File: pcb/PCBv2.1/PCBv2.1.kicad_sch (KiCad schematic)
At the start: 50 parts, among them J1 USB4105-GF-A, J2 Conn_01x04, J3 Conn_01x04, J4 Conn_01x08, J5 Conn_01x08, SW1 SW_Push, SW2 SW_Push, U1 STM32F411CEUx, U2 BNO055, U3 AP2112K-3.3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

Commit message: Add button part numbers for pcb
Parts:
- SW1, SW2: footprint (none) -> Button_Switch_SMD:SW_SPST_PTS810; Part Number (none) -> PTS810SJM250SMTRLFS
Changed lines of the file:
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@@
       (effects (font (size 1.27 1.27)) hide)
     )
-    (property "Footprint" "" (id 2) (at 92.71 34.29 0)
-      (effects (font (size 1.27 1.27)) hide)
-    )
-    (property "Datasheet" "~" (id 3) (at 92.71 34.29 0)
-      (effects (font (size 1.27 1.27)) hide)
-    )
-    (property "Part Number" "~" (id 4) (at 92.71 39.37 0)
+    (property "Footprint" "Button_Switch_SMD:SW_SPST_PTS810" (id 2) (at 92.71 34.29 0)
+      (effects (font (size 1.27 1.27)) hide)
+    )
+    (property "Datasheet" "https://www.mouser.com/datasheet/2/240/pts810-3050339.pdf" (id 3) (at 92.71 34.29 0)
+      (effects (font (size 1.27 1.27)) hide)
+    )
+    (property "Part Number" "PTS810SJM250SMTRLFS" (id 4) (at 92.71 39.37 0)
       (effects (font (size 1.27 1.27)) hide)
     )
@@
       (effects (font (size 1.27 1.27)) hide)
     )
-    (property "Footprint" "" (id 2) (at 107.95 16.51 0)
-      (effects (font (size 1.27 1.27)) hide)
-    )
-    (property "Datasheet" "~" (id 3) (at 107.95 16.51 0)
-      (effects (font (size 1.27 1.27)) hide)
-    )
-    (property "Part Number" "~" (id 4) (at 107.95 21.59 0)
+    (property "Footprint" "Button_Switch_SMD:SW_SPST_PTS810" (id 2) (at 107.95 16.51 0)
+      (effects (font (size 1.27 1.27)) hide)
+    )
+    (property "Datasheet" "https://www.mouser.com/datasheet/2/240/pts810-3050339.pdf" (id 3) (at 107.95 16.51 0)
+      (effects (font (size 1.27 1.27)) hide)
+    )
+    (property "Part Number" "PTS810SJM250SMTRLFS" (id 4) (at 107.95 21.59 0)
       (effects (font (size 1.27 1.27)) hide)
     )
@@
     )
     (path "/833c6f12-9e24-43f0-b3a0-e54ccab04f6f"
-      (reference "SW1") (unit 1) (value "SW_Push") (footprint "")
+      (reference "SW1") (unit 1) (value "SW_Push") (footprint "Button_Switch_SMD:SW_SPST_PTS810")
     )
     (path "/c2428200-dffb-4a56-a43e-092f070c9e0f"
-      (reference "SW2") (unit 1) (value "SW_Push") (footprint "")
+      (reference "SW2") (unit 1) (value "SW_Push") (footprint "Button_Switch_SMD:SW_SPST_PTS810")
     )
     (path "/3b913be8-1b8c-4023-a733-8403685bfb07"

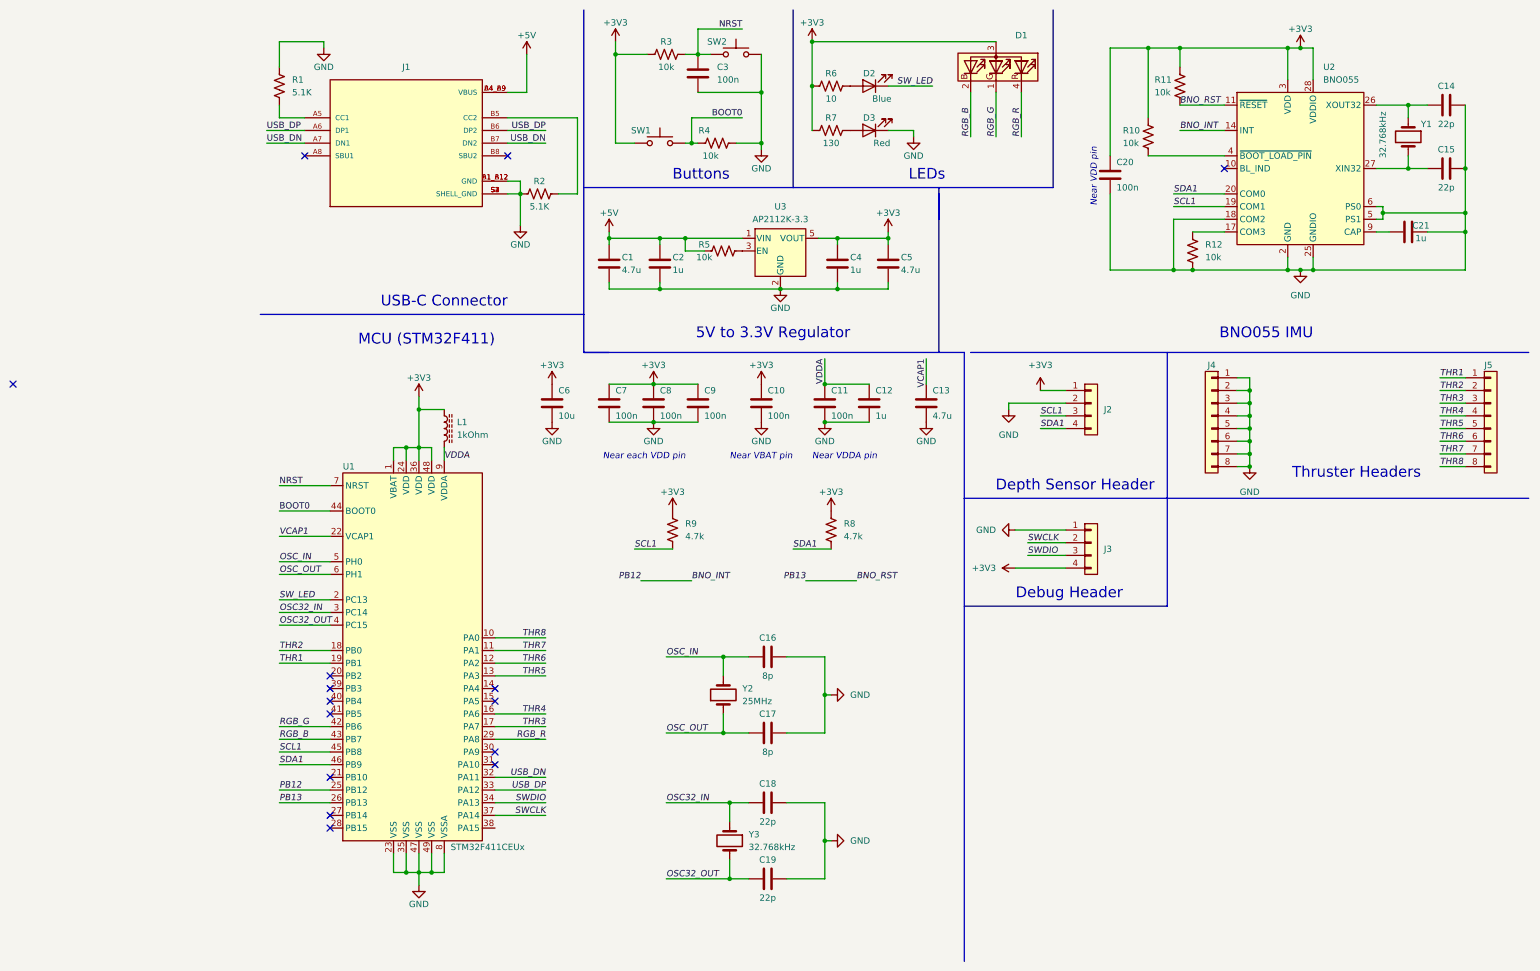
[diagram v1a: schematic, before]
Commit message: Add crystal part numbers to pcb
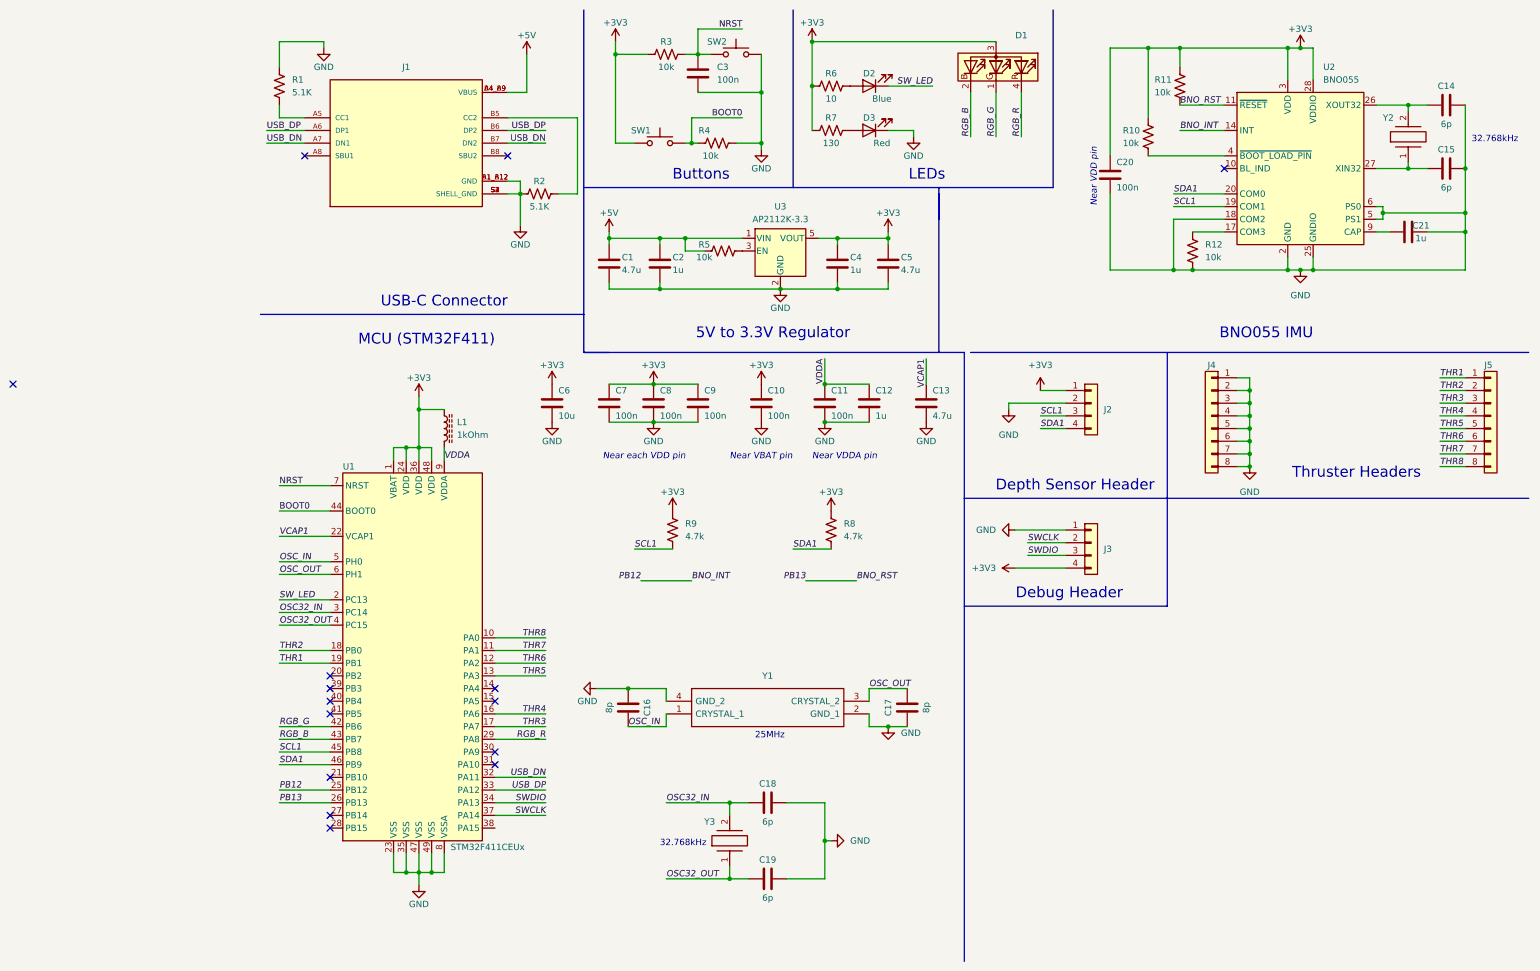
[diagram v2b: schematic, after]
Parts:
- removed Y1, Y3: 32.768kHz, symbol Device:Crystal
- removed Y2: 25MHz, symbol Device:Crystal
- added Y1: NX2016SA-25.000M-STD-CZS-1, NX2016SA32MEXS00ACS06465, symbol cboard:NX2016SA-25.000M-STD-CZS-1
- added Y2, Y3: NX3215SA-32.768K-STD-MUA-14, NX3215SA32768KSTDMUA14, symbol cboard:NX3215SA-32.768K-STD-MUA-14
- C14, C15, C18, C19: value 22p -> 6p; Part Number GRM21A5C2E220FW01D -> GQM2195G2H6R0CB12D
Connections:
- net GND: now also C16.1, C17.1, Y1.2 (GND_1), Y1.4 (GND_2); no longer C16.2, C17.2
- net OSC32_IN: now also Y3.2
- net OSC32_OUT: now also Y3.1
- net OSC_IN: now also C16.2, Y1.1 (CRYSTAL_1); no longer C16.1
- net OSC_OUT: now also C17.2, Y1.3 (CRYSTAL_2); no longer C17.1
- net at C14.1, U2.26 (XOUT32): now also Y2.2
- net at C15.1, U2.27 (XIN32): now also Y2.1
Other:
- note added: "25MHz"
- note added: "32.768kHz"
